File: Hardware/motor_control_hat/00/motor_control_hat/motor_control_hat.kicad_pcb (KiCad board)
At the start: 4 copper layers, 115 x 100 mm, 34 parts, among them P1 TB_1x2_5.08mm_RA, P10 X9254WR-04-N0SN, P11 X9254WR-04-N0SN, P12 X9254WR-04-N0SN, P13 X9254WR-04-N0SN, P2 TB_1x2_5.08mm_RA, P3 TB_1x2_5.08mm_RA, P4 TB_1x2_5.08mm_RA, P5 X9254WR-04-N0SN, P6 X9254WR-04-N0SN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

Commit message: Power connectors removed
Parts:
- removed P2, P3, P4: TB_1x2_5.08mm_RA, PluggableTerminalBLock:MX2EDGR-5.08-GN01-02P-Cu-A
- moved P1 80.2 mm to (153.0, 126.4), turned to 0 degrees
- moved P7 60.0 mm to (93.8, 126.4)
- moved P5 20.0 mm to (113.8, 126.4)
- moved P6 12.5 mm to (136.3, 126.4)
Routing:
- net /USART3_TX: track 103.2 -> 74.8 mm
- net /USART3_RX: track 96.0 -> 70.0 mm
- net /OC_IN_1: track 93.7 -> 75.8 mm
- net /OC_IN_2: track 58.2 -> 48.3 mm
- net /ENC3_PHA: track 128.5 -> 130.6 mm
- net GND: vias 279 -> 184
- net +24V: vias 159 -> 11
- removed copper zone on B.Cu, net +24V
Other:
- board size 115 x 100 mm -> 100 x 100 mm
- board text removed: "+24V"
- board text removed: "INPUT"

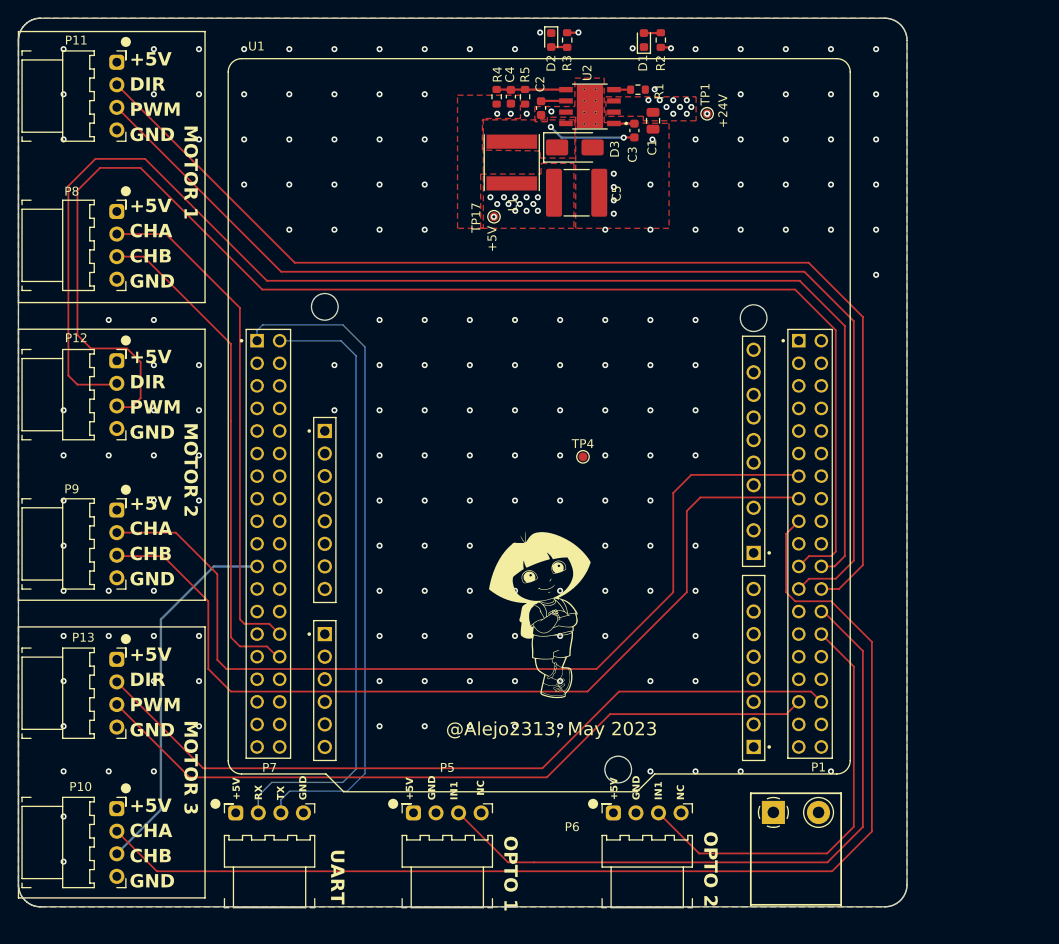
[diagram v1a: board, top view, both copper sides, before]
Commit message: Connectors changed. New power distribution board
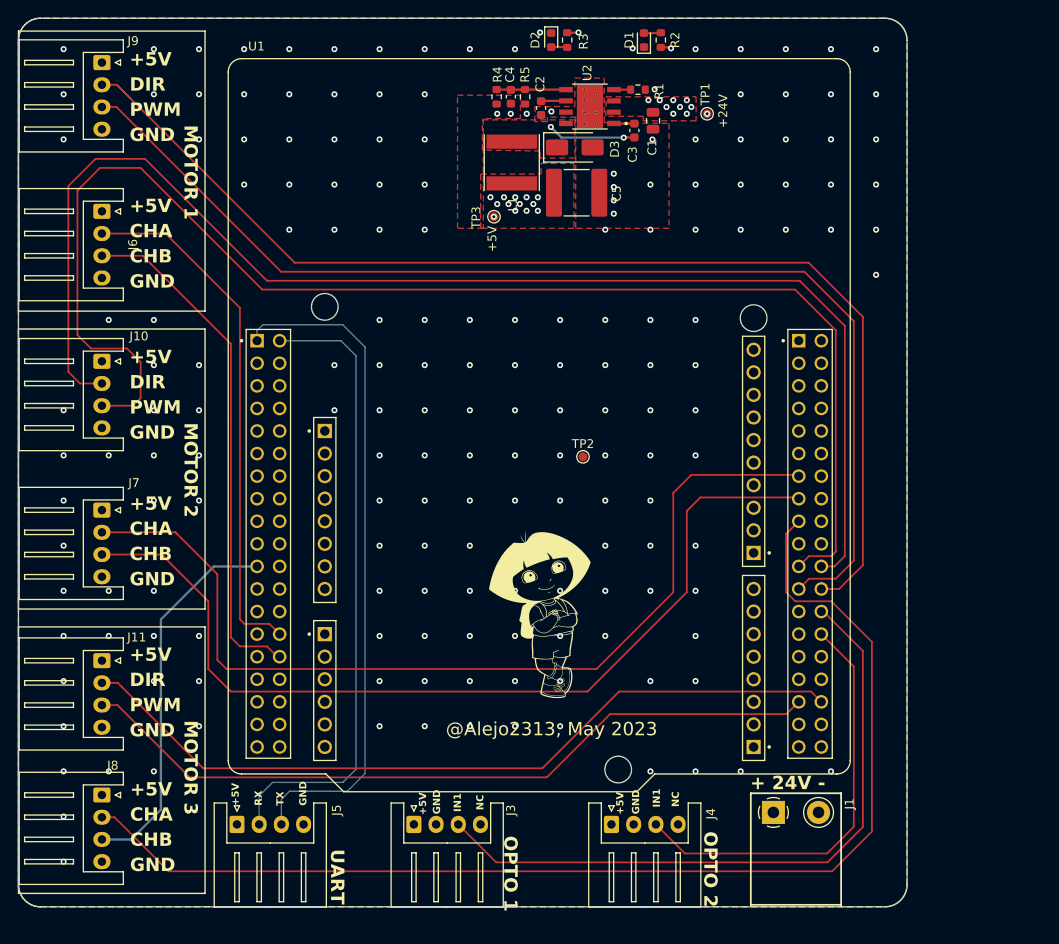
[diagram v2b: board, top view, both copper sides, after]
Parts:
- removed P10, P11, P12, P13, P5, P6, P7, P8, P9: X9254WR-04-N0SN, CustomConnectors:X9254WR-04-N0SN
- added J10: S4B-XH-A(LF)(SN), Connector_JST:JST_XH_S4B-XH-A_1x04_P2.50mm_Horizontal, F.Cu at (74.9, 75.6)
- added J11: S4B-XH-A(LF)(SN), Connector_JST:JST_XH_S4B-XH-A_1x04_P2.50mm_Horizontal, F.Cu at (74.9, 109.3)
- added J3: S4B-XH-A(LF)(SN), Connector_JST:JST_XH_S4B-XH-A_1x04_P2.50mm_Horizontal, F.Cu at (110.0, 127.7)
- added J4: S4B-XH-A(LF)(SN), Connector_JST:JST_XH_S4B-XH-A_1x04_P2.50mm_Horizontal, F.Cu at (132.2, 127.7)
- added J5: S4B-XH-A(LF)(SN), Connector_JST:JST_XH_S4B-XH-A_1x04_P2.50mm_Horizontal, F.Cu at (90.1, 127.7)
- added J6: S4B-XH-A(LF)(SN), Connector_JST:JST_XH_S4B-XH-A_1x04_P2.50mm_Horizontal, F.Cu at (74.9, 58.7)
- added J7: S4B-XH-A(LF)(SN), Connector_JST:JST_XH_S4B-XH-A_1x04_P2.50mm_Horizontal, F.Cu at (74.9, 92.4)
- added J8: S4B-XH-A(LF)(SN), Connector_JST:JST_XH_S4B-XH-A_1x04_P2.50mm_Horizontal, F.Cu at (74.9, 124.4)
- added J9: S4B-XH-A(LF)(SN), Connector_JST:JST_XH_S4B-XH-A_1x04_P2.50mm_Horizontal, F.Cu at (74.9, 42.0)
- renumbered P1 to J1, TP4 to TP2, TP17 to TP3
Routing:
- net /PWM_DIR_1: track 128.5 -> 132.4 mm
- net /ENC3_PHA: track 130.6 -> 132.9 mm
- net /PWM_DIR_2: track 152.7 -> 150.7 mm
- net /ENC2_PHA: track 104.4 -> 106.3 mm
- net /ENC1_PHB: track 56.3 -> 58.0 mm
- net /ENC2_PHB: track 102.0 -> 103.7 mm
- net /ENC1_PHA: track 57.5 -> 59.2 mm
- net /PWM_CH_1: track 127.4 -> 129.1 mm
- net /PWM_CH_3: track 83.7 -> 85.3 mm
- net /PWM_DIR_3: track 87.4 -> 89.0 mm
- net /PWM_CH_2: track 155.6 -> 157.1 mm
- net /USART3_TX: track 74.8 -> 76.0 mm
- net /USART3_RX: track 70.0 -> 71.2 mm
- net /ENC3_PHB: track 41.7 -> 42.7 mm
- net /OC_IN_1: track 75.8 -> 75.3 mm
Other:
- board text added: "+ 24V -"
